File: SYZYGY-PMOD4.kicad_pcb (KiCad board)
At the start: 2 copper layers, 45 x 60 mm, 38 parts, among them J1 PMOD1, J2 PMOD2, J3 PMOD3, J4 PMOD4, J5 QTE-020-01-F-D-A, J6 ISP, U1 ATtiny44-20SS

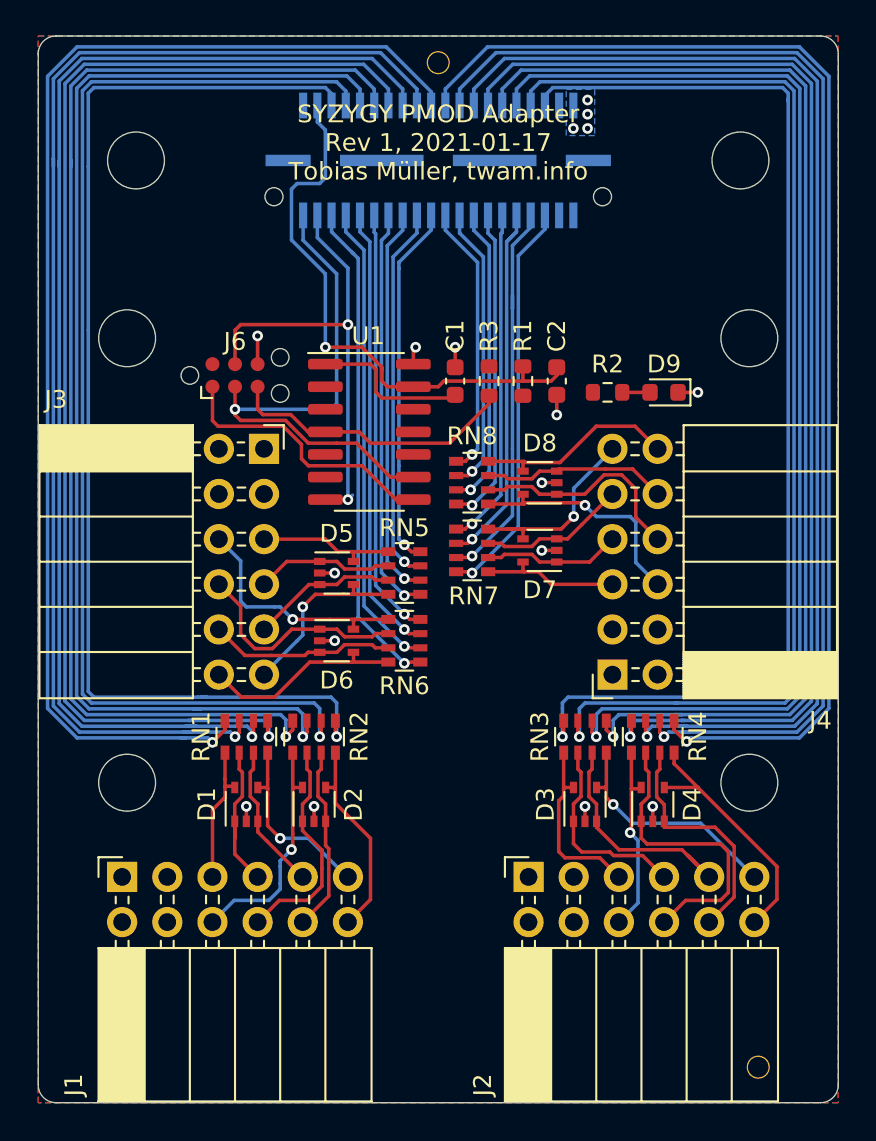
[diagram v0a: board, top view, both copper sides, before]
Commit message: Update to KiCad 6
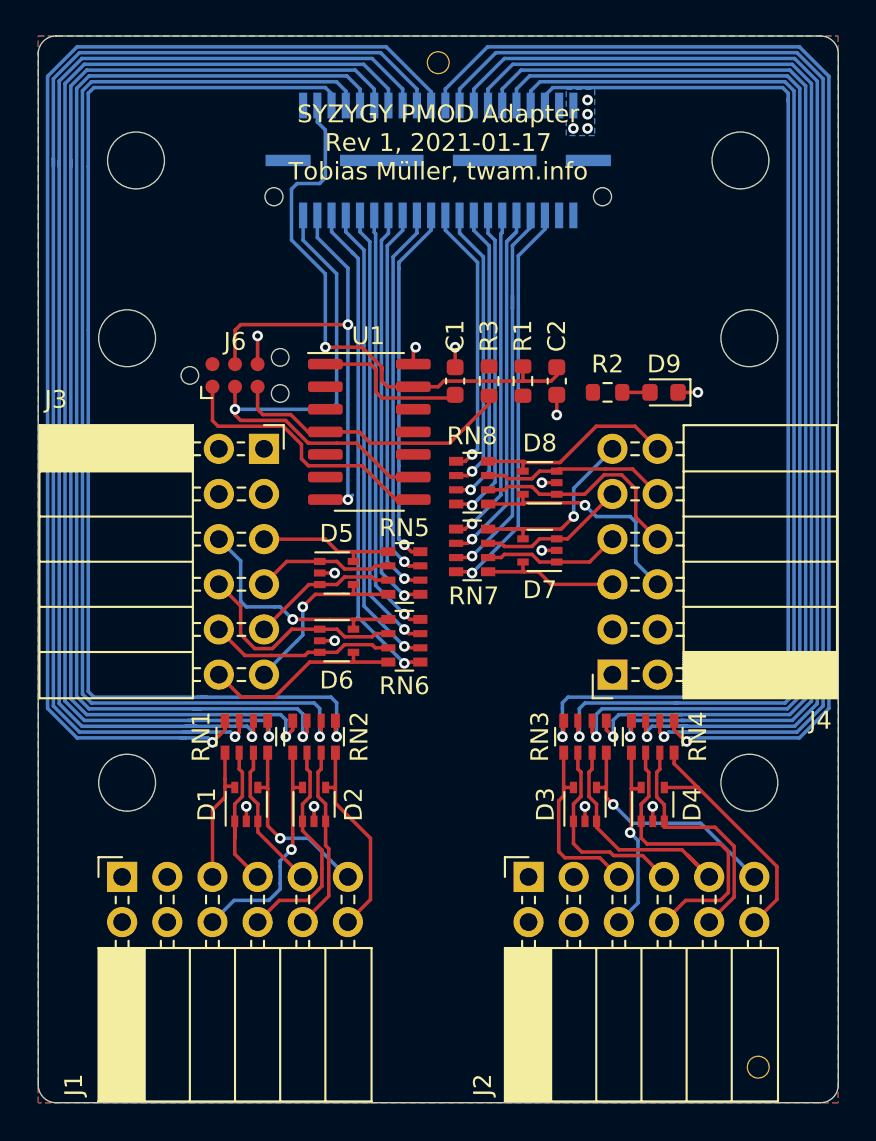
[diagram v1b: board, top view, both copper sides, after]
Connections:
- net /~RESET renamed /~{RESET}
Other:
- net class Default removed
